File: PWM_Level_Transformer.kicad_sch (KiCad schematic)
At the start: 5 parts

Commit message: Первая версия в производство
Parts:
- added R42, R47: 10k, Resistor_SMD:R_0805_2012Metric_Pad1.20x1.40mm_HandSolder, symbol Device:R_Small
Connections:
- net GND: now also R42.1, R47.2
- net nERR_IN: now reaches D8.4 (Bout)
- net nERR_IN_GPIO: now reaches D8.5 (Bin)
- net nERR_IN_GPIO: now also R42.2
- net RESET: now reaches D8.6 (Cout)
- net RESET_GPIO: now reaches D8.7 (Cin)
- net RESET_GPIO: now also R47.1
- no-connect marks 10 -> 6
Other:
- moved on the sheet: C24, R21

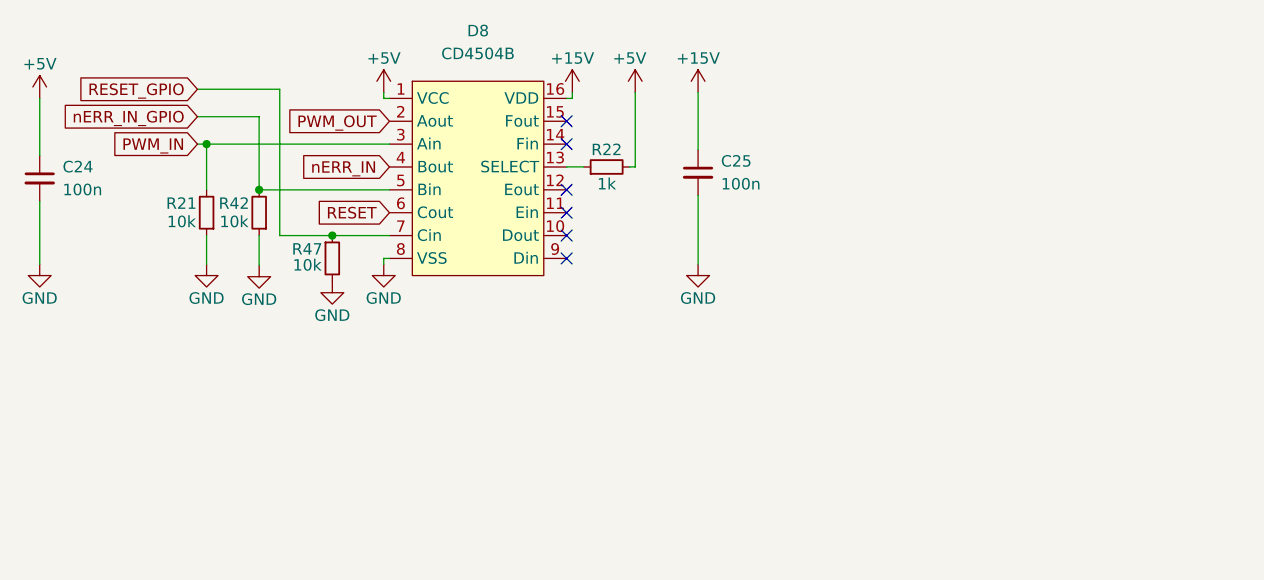
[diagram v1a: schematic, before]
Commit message: Добавил температуру, убрал подтяжки RS-485, заменил ШИМ на дифференциальный сигнал, добавил земли RS-485
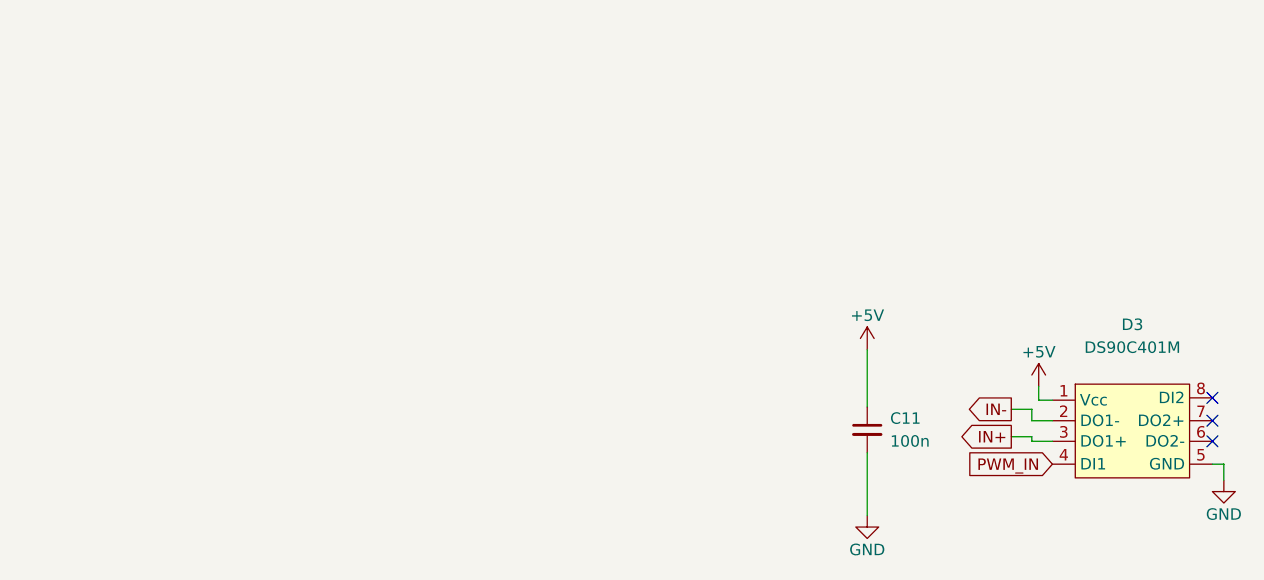
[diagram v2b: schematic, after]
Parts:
- removed C24, C25: 100n, Capacitor_SMD:C_0805_2012Metric_Pad1.18x1.45mm_HandSolder, symbol Device:C_Small
- removed D8: CD4504B, Package_SO:SOP-16_3.9x9.9mm_P1.27mm, symbol Level_Transformer:CD4504B
- removed R21, R42, R47: 10k, Resistor_SMD:R_0805_2012Metric_Pad1.20x1.40mm_HandSolder, symbol Device:R_Small
- removed R22: 1k, Resistor_SMD:R_0805_2012Metric_Pad1.20x1.40mm_HandSolder, symbol Device:R_Small
- added C11: 100n, Capacitor_SMD:C_0805_2012Metric_Pad1.18x1.45mm_HandSolder, symbol Device:C_Small
- added D3: DS90C401M, Package_SO:SOIC-8_3.9x4.9mm_P1.27mm, symbol My_Tranciever:DS90C401M
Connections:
- net +5V: now also C11.1, D3.1 (Vcc)
- net GND: now also C11.2, D3.5 (GND)
- net PWM_IN: now also D3.4 (DI1)
- new net IN+: D3.3 (DO1+)
- new net IN-: D3.2 (DO1-)
- no-connect marks 6 -> 3
